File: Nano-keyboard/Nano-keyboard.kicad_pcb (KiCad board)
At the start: 2 copper layers, 17.8 x 43.2 mm, 31 parts, among them P1 Digital, P2 Analog, P3 CONN_01X01, P4 CONN_01X01, P5 CONN_01X01, P6 CONN_01X01

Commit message: First layout design
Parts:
- moved B4 133.0 mm to (226.1, 114.3)
- moved D6 117.4 mm to (160.0, 105.4), turned to 90 degrees
- moved D10 111.8 mm to (160.0, 85.1), turned to 90 degrees
- moved B8 92.5 mm to (226.1, 91.4)
- moved B7 82.4 mm to (200.7, 91.4)
- moved D7 78.0 mm to (185.4, 105.4), turned to 90 degrees
- moved D5 70.4 mm to (134.6, 105.4), turned to 90 degrees
- moved D9 70.1 mm to (134.6, 85.1), turned to 90 degrees
- moved B12 68.6 mm to (226.1, 71.1)
- moved D2 66.3 mm to (160.0, 128.3), turned to 90 degrees
- moved D12 63.9 mm to (210.8, 85.1), turned to 90 degrees
- moved D11 63.0 mm to (185.4, 85.1), turned to 90 degrees
- moved B9 59.3 mm to (149.9, 71.1)
- moved D8 50.3 mm to (210.8, 105.4), turned to 90 degrees
- moved B11 48.3 mm to (200.7, 71.1)
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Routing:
- net /ROW1: track 0.00 -> 127.4 mm
- net /ROW2: track 0.00 -> 103.3 mm
- net /ROW3: track 0.00 -> 92.7 mm
- net /FUNC: track 0.00 -> 56.2 mm
- net +3V3: track 0.00 -> 53.2 mm
- net Net-(B12-Pad1): track 0.00 -> 25.5 mm
- net Net-(B11-Pad1): track 0.00 -> 25.5 mm
- net Net-(B8-Pad1): track 0.00 -> 25.5 mm
- net Net-(B7-Pad1): track 0.00 -> 25.5 mm
- net Net-(B4-Pad1): track 0.00 -> 25.5 mm
- net Net-(B3-Pad1): track 0.00 -> 25.5 mm
- net Net-(B9-Pad1): track 0.00 -> 25.5 mm
- net Net-(B5-Pad1): track 0.00 -> 25.5 mm
- net Net-(B1-Pad1): track 0.00 -> 25.5 mm
- net Net-(B10-Pad1): track 0.00 -> 25.5 mm
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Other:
- outline, holes or cut-outs redrawn

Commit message: ESP initial changes
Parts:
- removed P1: Digital, Socket_Arduino_Nano:Socket_Strip_Arduino_1x15
- removed P2: Analog, Socket_Arduino_Nano:Socket_Strip_Arduino_1x15
- removed P3, P4, P5, P6: CONN_01X01, Socket_Arduino_Nano:1pin_Nano
- added LED0: LRTBGVSR-U4V2-JW+A6BB-D8+S2U2-7Z-20-S, lib:LRTBGVSRU4V2JWA6BBD8S2U27Z20S, F.Cu at (83.2, 119.4)
- added LED1: LRTBGVSR-U4V2-JW+A6BB-D8+S2U2-7Z-20-S, lib:LRTBGVSRU4V2JWA6BBD8S2U27Z20S, F.Cu at (116.2, 119.4)
- added LED10: LRTBGVSR-U4V2-JW+A6BB-D8+S2U2-7Z-20-S, lib:LRTBGVSRU4V2JWA6BBD8S2U27Z20S, F.Cu at (142.9, 73.7)
- added LED11: LRTBGVSR-U4V2-JW+A6BB-D8+S2U2-7Z-20-S, lib:LRTBGVSRU4V2JWA6BBD8S2U27Z20S, F.Cu at (168.4, 73.9)
- added LED12: LRTBGVSR-U4V2-JW+A6BB-D8+S2U2-7Z-20-S, lib:LRTBGVSRU4V2JWA6BBD8S2U27Z20S, F.Cu at (193.7, 73.7)
- added LED2: LRTBGVSR-U4V2-JW+A6BB-D8+S2U2-7Z-20-S, lib:LRTBGVSRU4V2JWA6BBD8S2U27Z20S, F.Cu at (141.6, 119.4)
- added LED3: LRTBGVSR-U4V2-JW+A6BB-D8+S2U2-7Z-20-S, lib:LRTBGVSRU4V2JWA6BBD8S2U27Z20S, F.Cu at (167.0, 119.4)
- added LED4: LRTBGVSR-U4V2-JW+A6BB-D8+S2U2-7Z-20-S, lib:LRTBGVSRU4V2JWA6BBD8S2U27Z20S, F.Cu at (192.4, 119.4)
- added LED5: LRTBGVSR-U4V2-JW+A6BB-D8+S2U2-7Z-20-S, lib:LRTBGVSRU4V2JWA6BBD8S2U27Z20S, F.Cu at (116.2, 96.5)
- added LED6: LRTBGVSR-U4V2-JW+A6BB-D8+S2U2-7Z-20-S, lib:LRTBGVSRU4V2JWA6BBD8S2U27Z20S, F.Cu at (141.6, 96.5)
- added LED7: LRTBGVSR-U4V2-JW+A6BB-D8+S2U2-7Z-20-S, lib:LRTBGVSRU4V2JWA6BBD8S2U27Z20S, F.Cu at (167.0, 96.5)
- added LED8: LRTBGVSR-U4V2-JW+A6BB-D8+S2U2-7Z-20-S, lib:LRTBGVSRU4V2JWA6BBD8S2U27Z20S, F.Cu at (192.4, 96.5)
- added LED9: LRTBGVSR-U4V2-JW+A6BB-D8+S2U2-7Z-20-S, lib:LRTBGVSRU4V2JWA6BBD8S2U27Z20S, F.Cu at (117.5, 73.7)
- added U2: ESP32-WROOM-32, RF_Module:ESP32-WROOM-32, F.Cu at (88.9, 86.5)
- moved B1 32.7 mm to (118.7, 124.5)
- moved B3 32.7 mm to (169.5, 124.5)
- moved B4 32.7 mm to (194.9, 124.5)
- moved B5 32.7 mm to (118.7, 101.6)
- moved B7 32.7 mm to (169.5, 101.6)
- moved B8 32.7 mm to (194.9, 101.6)
- moved D1 32.7 mm to (103.5, 138.4)
- moved D2 32.7 mm to (128.9, 138.4)
- moved D5 32.7 mm to (103.5, 115.6)
- moved D6 32.7 mm to (128.9, 115.6)
- moved B0 32.7 mm to (78.1, 127.0)
- moved B2 32.7 mm to (144.1, 124.5)
- moved B6 32.7 mm to (144.1, 101.6)
- moved D3 32.7 mm to (154.3, 138.4)
- moved D4 32.7 mm to (179.7, 138.4)
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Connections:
- net /COL1 renamed COL1
- net /COL2 renamed COL2
- net /COL3 renamed COL3
- net /COL4 renamed COL4
- net /ROW1 renamed ROW1
- net /ROW2 renamed ROW2
- net /ROW3 renamed ROW3
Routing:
- net /FUNC: track 56.2 -> 0.00 mm
- net +3V3: track 53.2 -> 0.00 mm
- net ROW1: track 127.4 -> 76.2 mm
- net ROW2: track 103.3 -> 76.2 mm
- net ROW3: track 92.7 -> 76.2 mm
- net (no net): vias 0 -> 4
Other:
- board size 17.8 x 43.2 mm -> 143.3 x 80.2 mm
- board text removed: "1"

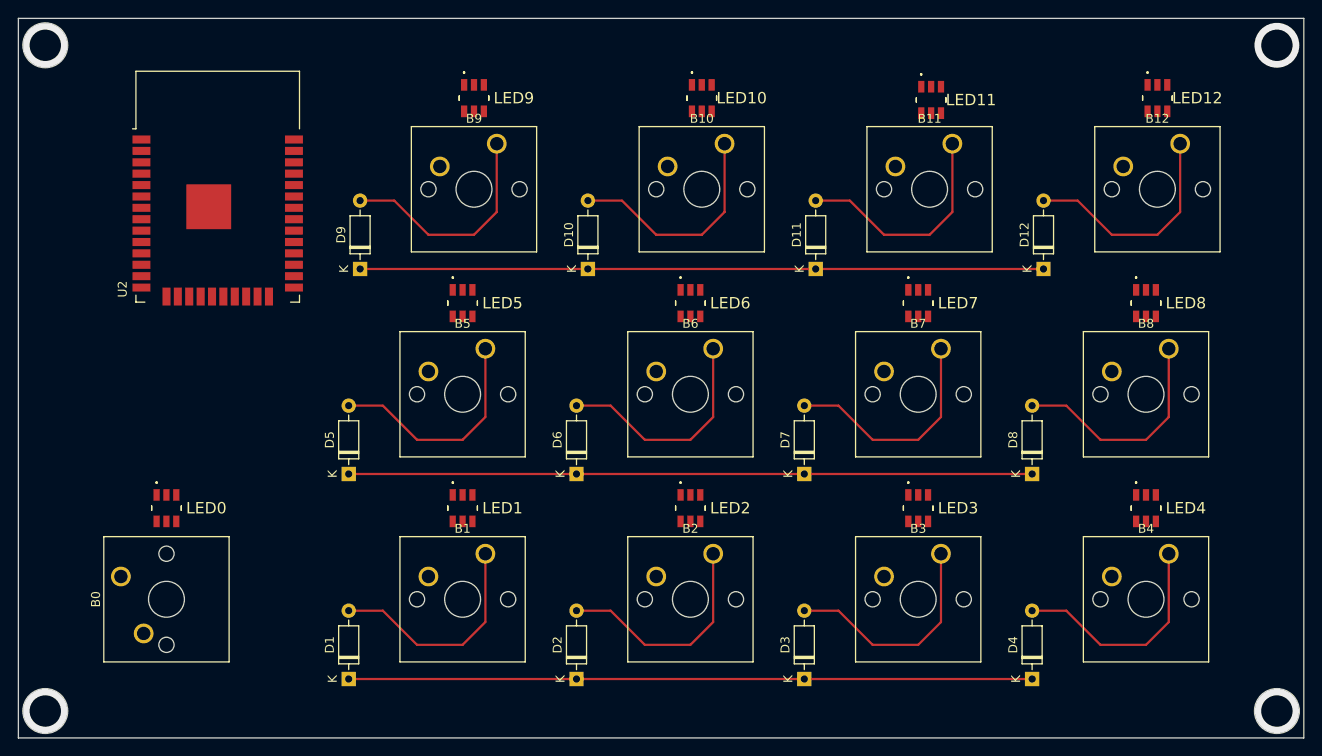
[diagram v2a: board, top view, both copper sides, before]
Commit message: Minor schematic changes
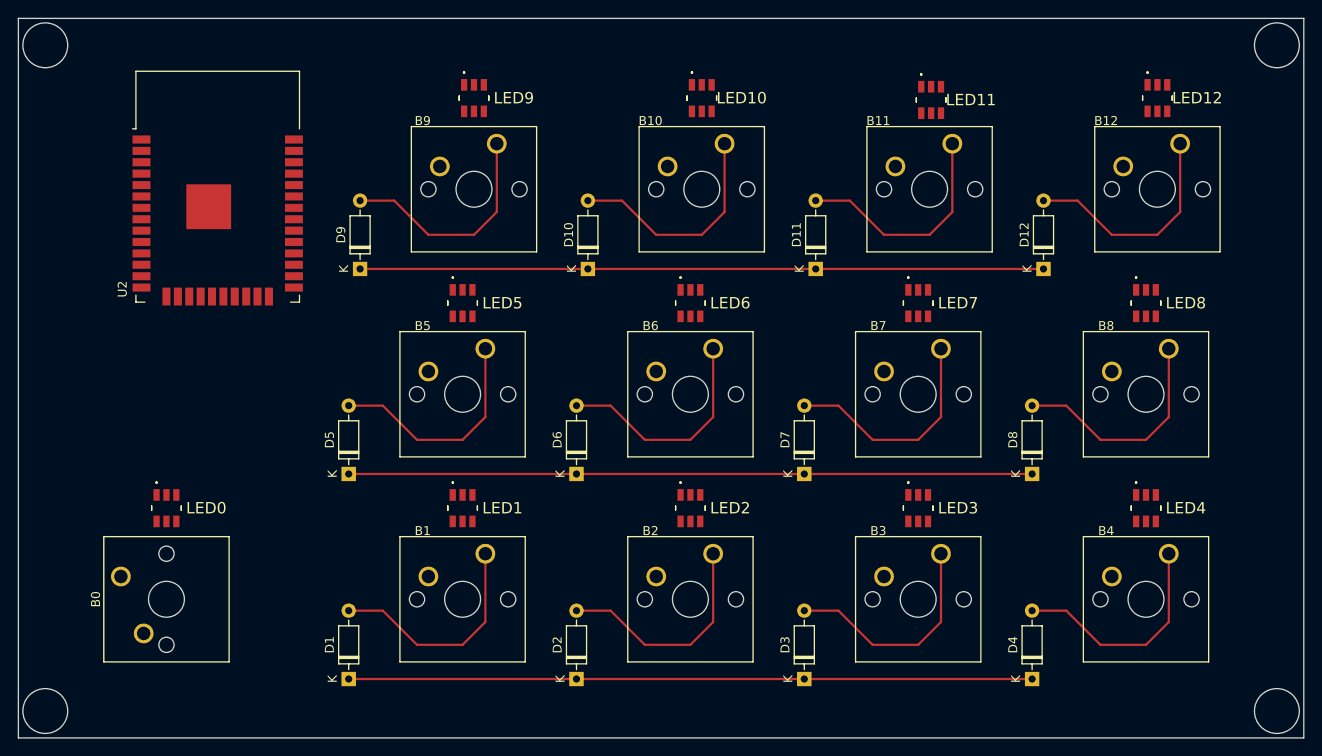
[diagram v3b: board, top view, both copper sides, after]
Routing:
- net (no net): vias 4 -> 0
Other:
- outline, holes or cut-outs redrawn

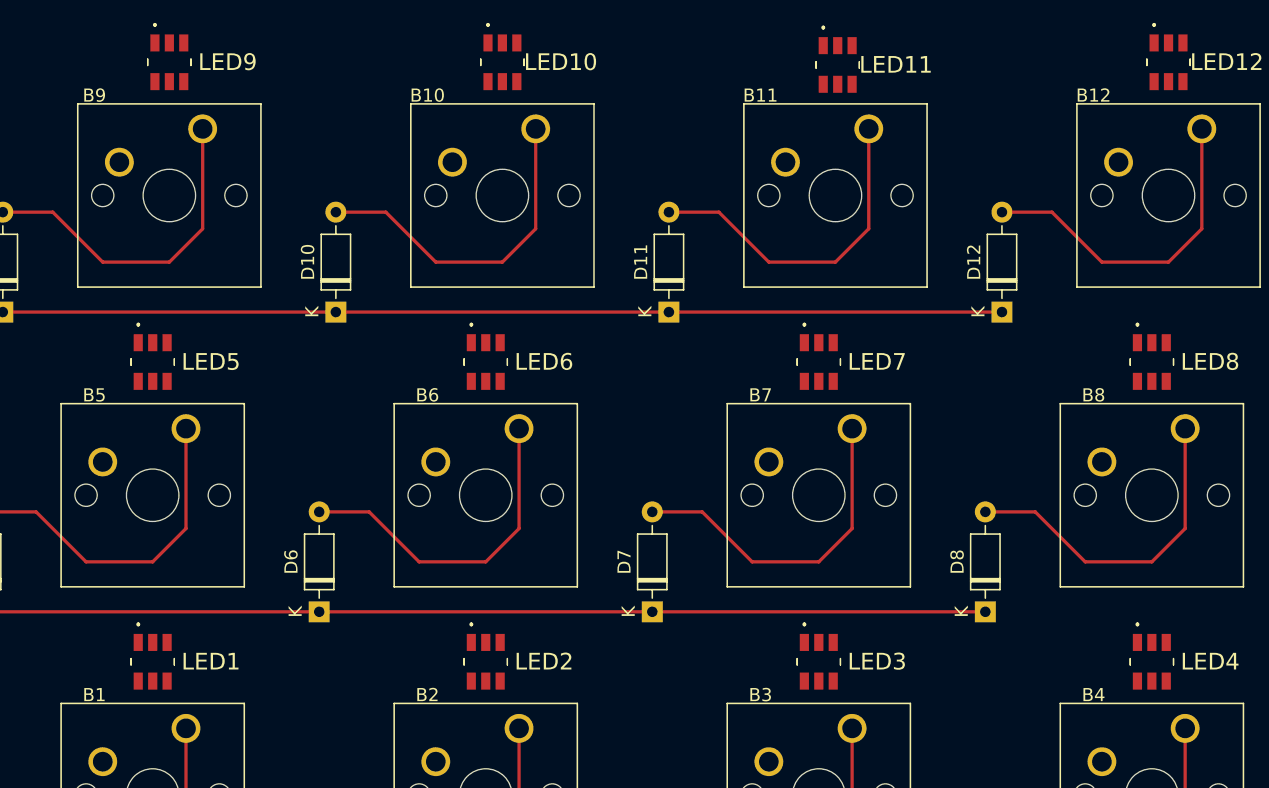
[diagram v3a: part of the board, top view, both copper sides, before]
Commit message: 3D Switch Models
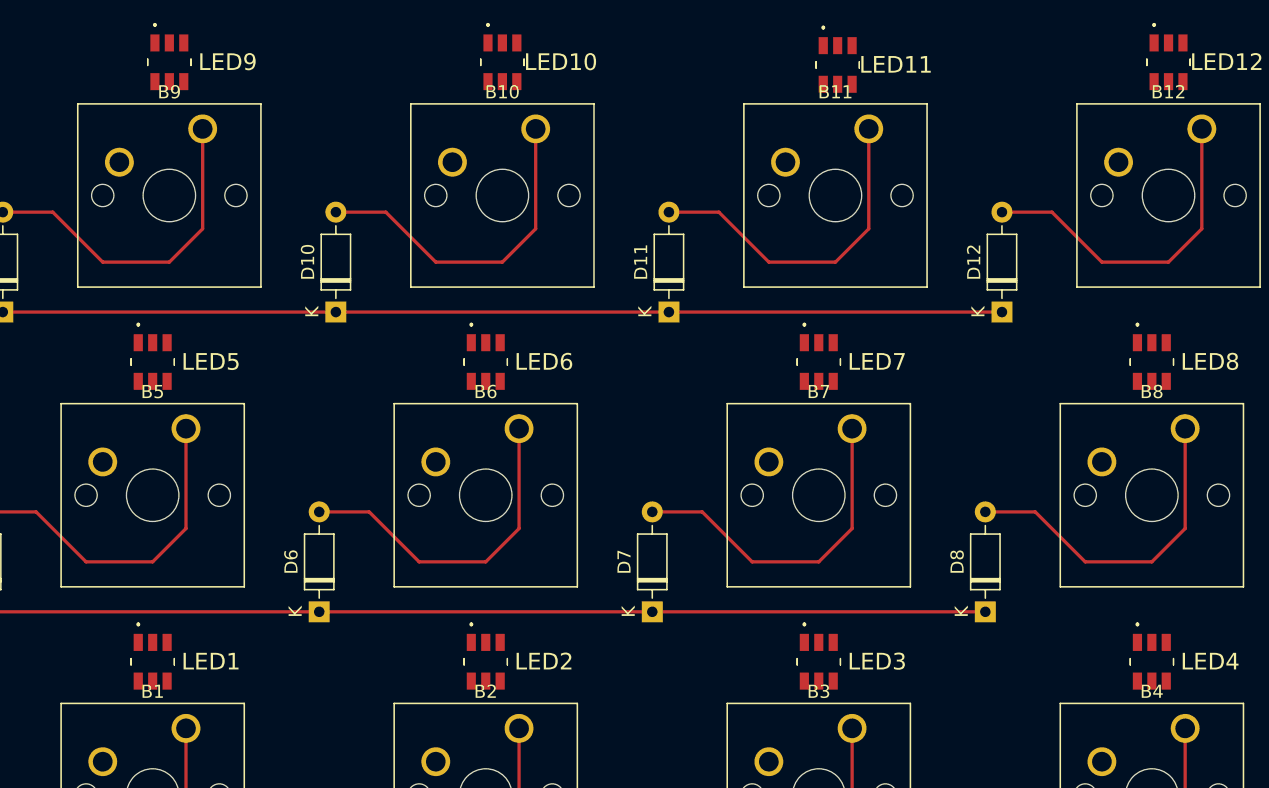
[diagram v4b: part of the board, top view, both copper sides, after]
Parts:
- B1, B10, B11, B12, B2, B3, B4, B5, B6, B7, B8, B9: footprint Button_Switch_Keyboard:SW_Cherry_MX_1.00u_PCB -> lib:SW_Cherry_MX_1.00u_PCB

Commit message: Minor changes
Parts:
- added U1: QBC847BL, lib:SOT96P237X111-3N, F.Cu at (92.7, 105.4)
- added U3: QBC847BL, lib:SOT96P237X111-3N, F.Cu at (82.9, 105.4)
- added U4: QBC847BL, lib:SOT96P237X111-3N, F.Cu at (87.8, 105.4)
- B0: footprint Button_Switch_Keyboard:SW_Cherry_MX_1.00u_PCB -> lib:SW_Cherry_MX_1.00u_PCB
- moved B0 11.1 mm to (88.9, 124.5), turned to 0 degrees
- moved LED0 3.17 mm to (86.4, 119.4)

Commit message: Diode Changes
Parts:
- D1, D10, D11, D12, D3, D4, D5, D6, D7, D8, D9: footprint Diode_THT:D_DO-35_SOD27_P7.62mm_Horizontal -> Diode_THT:D_DO-35_SOD27_P3.81mm_Vertical_AnodeUp

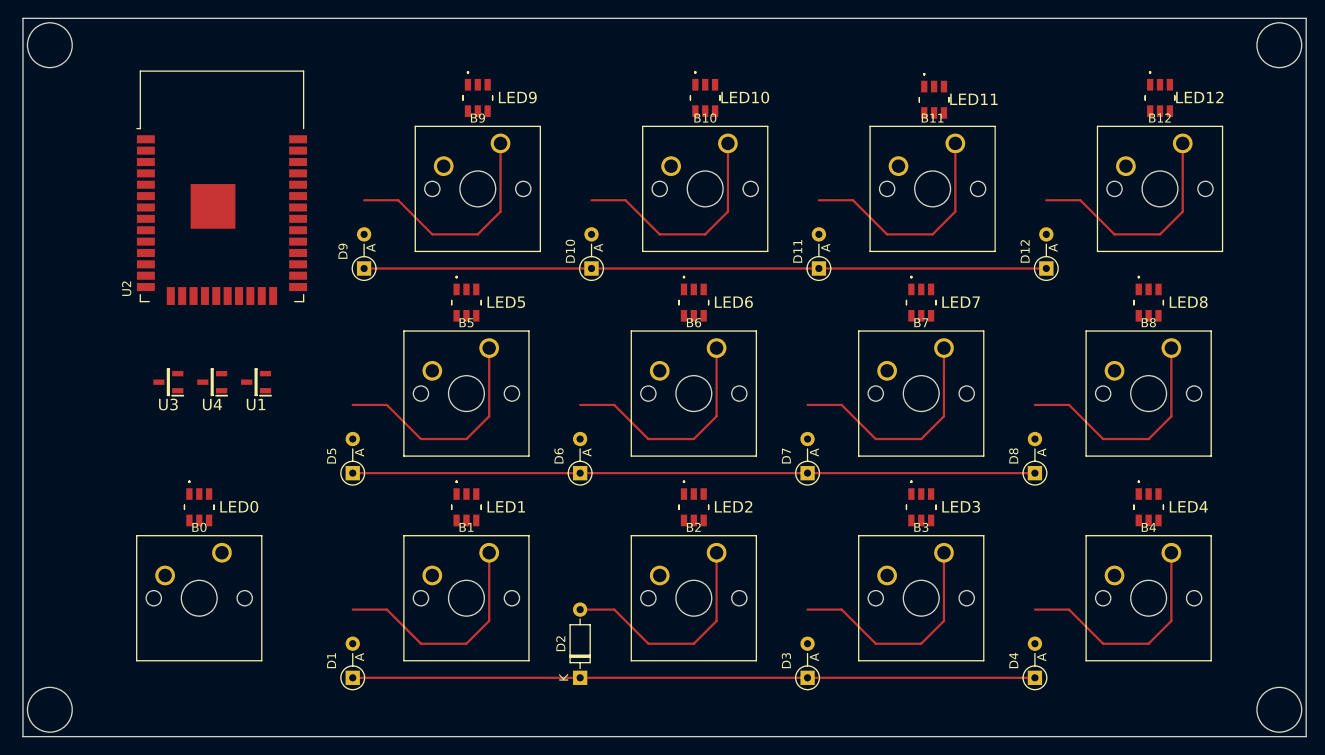
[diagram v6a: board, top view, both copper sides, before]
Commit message: Charger Module and keyboard layout changes
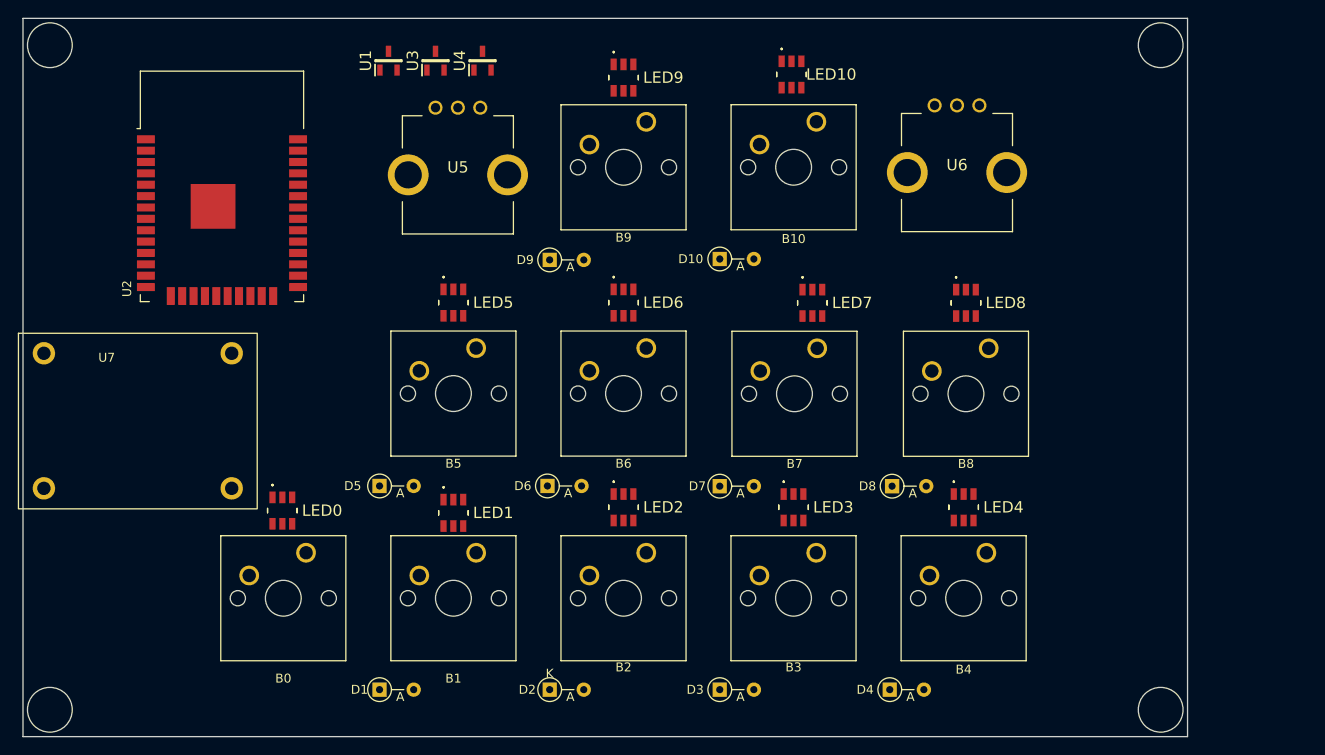
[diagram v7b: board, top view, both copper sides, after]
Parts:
- removed B11, B12: Cherry_Switch_1U_PCB, lib:SW_Cherry_MX_1.00u_PCB
- removed D11, D12: 1N914, Diode_THT:D_DO-35_SOD27_P3.81mm_Vertical_AnodeUp
- removed LED11, LED12: LRTBGVSR-U4V2-JW+A6BB-D8+S2U2-7Z-20-S, lib:LRTBGVSRU4V2JWA6BBD8S2U27Z20S
- added U5: EN12-HN22AF25, lib:EN12HN22AF25, F.Cu at (117.8, 74.8)
- added U6: EN12-HN22AF25, lib:EN12HN22AF25, F.Cu at (173.5, 74.5)
- added U7: TP4050, lib:TP4050-module, F.Cu at (77.2, 104.4)
- D2: footprint Diode_THT:D_DO-35_SOD27_P7.62mm_Horizontal -> Diode_THT:D_DO-35_SOD27_P3.81mm_Vertical_AnodeUp
- moved U4 46.9 mm to (118.0, 69.5), turned to 90 degrees
- moved U3 46.7 mm to (112.8, 69.5), turned to 90 degrees
- moved U1 38.8 mm to (107.5, 69.5), turned to 90 degrees
- moved D9 20.7 mm to (125.5, 91.8), turned to 0 degrees
- moved B4 20.7 mm to (174.3, 124.5)
- moved LED4 20.7 mm to (171.7, 119.4)
- moved B8 20.4 mm to (174.5, 101.6)
- moved LED8 20.4 mm to (172.0, 96.5)
- moved B9 16.5 mm to (136.3, 76.3)
- moved LED9 16.4 mm to (133.8, 71.4)
- moved D4 16.3 mm to (163.5, 139.8), turned to 0 degrees
- moved D8 16.0 mm to (163.8, 117.0), turned to 0 degrees
- moved D10 14.4 mm to (144.5, 91.7), turned to 0 degrees
- moved B3 14.3 mm to (155.3, 124.5)
- moved LED3 14.3 mm to (152.7, 119.4)
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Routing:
- net ROW2: track 76.2 -> 0.00 mm
- net ROW1: track 76.2 -> 0.00 mm
- net ROW3: track 76.2 -> 0.00 mm
- net Net-(B12-Pad1): track 25.5 -> 0.00 mm
- net Net-(B11-Pad1): track 25.5 -> 0.00 mm
- net Net-(B1-Pad1): track 25.5 -> 0.00 mm
- net Net-(B5-Pad1): track 25.5 -> 0.00 mm
- net Net-(B2-Pad1): track 25.5 -> 0.00 mm
- net Net-(B6-Pad1): track 25.5 -> 0.00 mm
- net Net-(B9-Pad1): track 25.5 -> 0.00 mm
- net Net-(B10-Pad1): track 25.5 -> 0.00 mm
- net Net-(B4-Pad1): track 25.5 -> 0.00 mm
- net Net-(B3-Pad1): track 25.5 -> 0.00 mm
- net Net-(B8-Pad1): track 25.5 -> 0.00 mm
- net Net-(B7-Pad1): track 25.5 -> 0.00 mm
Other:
- board size 143.3 x 80.2 mm -> 130.1 x 80.2 mm

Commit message: Layout changes
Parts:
- moved U2 5.30 mm to (88.5, 81.2)
- moved U7 5.02 mm to (77.7, 99.4)
- moved LED7 4.08 mm to (150.8, 96.6)
- moved D8 3.03 mm to (160.7, 117.0)
- moved B4 3.03 mm to (171.2, 124.5)
- moved B8 3.03 mm to (171.5, 101.6)
- moved D4 3.03 mm to (160.5, 139.8)
- moved LED4 3.03 mm to (168.7, 119.4)
- moved LED8 3.03 mm to (169.0, 96.5)
- moved U6 3.01 mm to (172.0, 77.1)
- moved B10 2.92 mm to (153.6, 78.7)
- moved LED10 2.92 mm to (150.8, 73.4)
- moved D10 2.92 mm to (142.8, 94.0)
- moved B9 2.47 mm to (135.5, 78.7)
- moved D9 2.47 mm to (124.8, 94.1)
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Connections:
- U1 pad 1: unconnected-(U1-Pad1) -> /LED_RED
- U2 pad 1: Net-(U2-Pad1) -> GND
- U2 pad 15: Net-(U2-Pad1) -> GND
- U2 pad 2: unconnected-(U2-Pad2) -> +3V3
- U2 pad 25: unconnected-(U2-Pad25) -> /BOOT
- U2 pad 38: Net-(U2-Pad1) -> GND
- U2 pad 39: Net-(U2-Pad1) -> GND
- U2 pad 6: unconnected-(U2-Pad6) -> /LED_GREEN
- U2 pad 7: unconnected-(U2-Pad7) -> /LED_BLUE
- U2 pad 9: unconnected-(U2-Pad9) -> /LED_RED
- U3 pad 1: unconnected-(U3-Pad1) -> /LED_GREEN
- U4 pad 1: unconnected-(U4-Pad1) -> /LED_BLUE
- U5 pad C1: unconnected-(U5-PadC1) -> Net-(U6-PadC1)
- U5 pad MH1: unconnected-(U5-PadMH1) -> GND
- U5 pad MH2: unconnected-(U5-PadMH2) -> GND
- U6 pad C1: unconnected-(U6-PadC1) -> Net-(U6-PadC1)
- U6 pad MH1: unconnected-(U6-PadMH1) -> GND
- U6 pad MH2: unconnected-(U6-PadMH2) -> GND
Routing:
- added copper zone on B.Cu, net GND
- added copper zone on F.Cu, net GND
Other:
- board size 130.1 x 80.2 mm -> 120.1 x 80.2 mm
- board text added: "Custom-macro-keypad v1.0 Design by Guilherme Freire"
- board text added: "github.com/Freireg/Custom-Macro-Keypad"
